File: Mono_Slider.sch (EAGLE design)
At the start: 6 parts

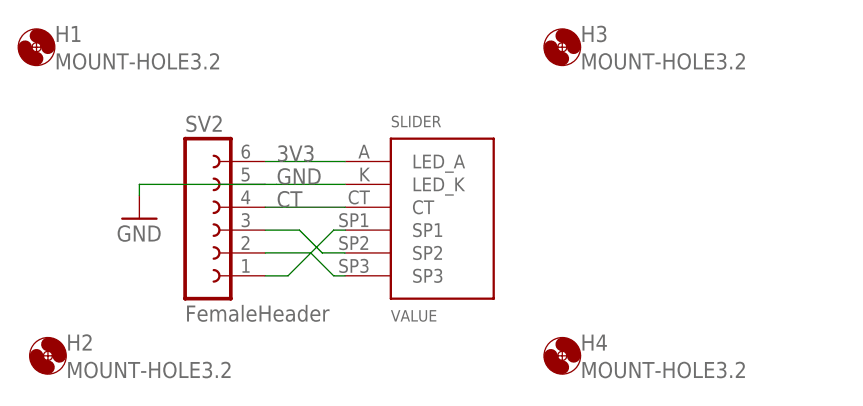
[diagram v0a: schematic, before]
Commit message: Made slider smaller.
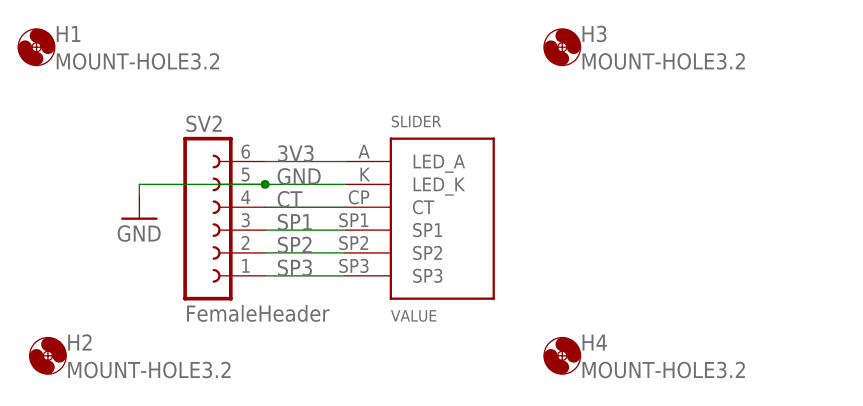
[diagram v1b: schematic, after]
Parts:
- SL1: device SLIDER:SLIDER -> SLIDER:SLIDERSLIDER_SMALL
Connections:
- removed net N$13: SL1.SP3, SV2.2
- removed net N$6: SL1.SP2, SV2.3
- removed net N$7: SL1.SP1, SV2.1
- new net SP1: SL1.SP1, SV2.3
- new net SP2: SL1.SP2, SV2.2
- new net SP3: SL1.SP3, SV2.1
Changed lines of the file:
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@@
 <setting verticaltext="up"/>
 </settings>
-<grid distance="1.27" unitdist="mm" unit="mm" style="dots" multiple="1" display="yes" altdistance="1.27" altunitdist="mm" altunit="mm"/>
+<grid distance="0.1" unitdist="inch" unit="inch" style="lines" multiple="1" display="no" altdistance="0.01" altunitdist="inch" altunit="inch"/>
 <layers>
 <layer number="1" name="Top" color="4" fill="1" visible="no" active="no"/>
@@
 </classes>
 <parts>
-<part name="SL1" library="SLIDER" deviceset="SLIDER" device="" value="SLIDER"/>
 <part name="SV2" library="con-lsta" deviceset="FE06-1" device="" value="FemaleHeader"/>
 <part name="H1" library="holes" deviceset="MOUNT-HOLE" device="3.2"/>
@@
 <part name="H4" library="holes" deviceset="MOUNT-HOLE" device="3.2"/>
 <part name="GND1" library="supply1" deviceset="GND" device=""/>
+<part name="SL1" library="SLIDER" deviceset="SLIDER" device="SLIDER_SMALL" value="SLIDER"/>
 </parts>
 <sheets>
@@
 </plain>
 <instances>
-<instance part="SL1" gate="G$1" x="78.74" y="58.42"/>
 <instance part="SV2" gate="G$1" x="50.8" y="57.15"/>
 <instance part="H1" gate="G$1" x="33.02" y="77.47"/>
@@
 <instance part="H4" gate="G$1" x="91.44" y="43.18"/>
 <instance part="GND1" gate="1" x="44.45" y="58.42"/>
+<instance part="SL1" gate="G$1" x="78.74" y="58.42"/>
 </instances>
 <busses>
@@
 <segment>
 <pinref part="SV2" gate="G$1" pin="6"/>
-<pinref part="SL1" gate="G$1" pin="LED_A"/>
 <wire x1="58.42" y1="64.77" x2="67.31" y2="64.77" width="0.1524" layer="91"/>
 <label x="59.69" y="64.77" size="1.778" layer="95"/>
+<pinref part="SL1" gate="G$1" pin="LED_A"/>
 </segment>
 </net>
@@
 <wire x1="44.45" y1="60.96" x2="44.45" y2="62.23" width="0.1524" layer="91"/>
 <pinref part="SV2" gate="G$1" pin="5"/>
+<label x="59.69" y="62.23" size="1.778" layer="95"/>
+<wire x1="58.42" y1="62.23" x2="67.31" y2="62.23" width="0.1524" layer="91"/>
+<wire x1="44.45" y1="62.23" x2="58.42" y2="62.23" width="0.1524" layer="91"/>
 <pinref part="SL1" gate="G$1" pin="LED_K"/>
-<wire x1="58.42" y1="62.23" x2="59.69" y2="62.23" width="0.1524" layer="91"/>
-<label x="59.69" y="62.23" size="1.778" layer="95"/>
-<wire x1="59.69" y1="62.23" x2="67.31" y2="62.23" width="0.1524" layer="91"/>
-<wire x1="44.45" y1="62.23" x2="58.42" y2="62.23" width="0.1524" layer="91"/>
+<junction x="58.42" y="62.23"/>
 </segment>
 </net>
@@
 <segment>
 <pinref part="SV2" gate="G$1" pin="4"/>
-<pinref part="SL1" gate="G$1" pin="CT"/>
 <wire x1="58.42" y1="59.69" x2="67.31" y2="59.69" width="0.1524" layer="91"/>
 <label x="59.69" y="59.69" size="1.778" layer="95"/>
+<pinref part="SL1" gate="G$1" pin="CT"/>
 </segment>
 </net>
-<net name="N$7" class="0">
+<net name="SP1" class="0">
 <segment>
+<pinref part="SV2" gate="G$1" pin="3"/>
 <pinref part="SL1" gate="G$1" pin="SP1"/>
-<wire x1="67.31" y1="57.15" x2="66.04" y2="57.15" width="0.1524" layer="91"/>
-<wire x1="66.04" y1="57.15" x2="60.96" y2="52.07" width="0.1524" layer="91"/>
-<pinref part="SV2" gate="G$1" pin="1"/>
-<wire x1="60.96" y1="52.07" x2="58.42" y2="52.07" width="0.1524" layer="91"/>
+<wire x1="58.42" y1="57.15" x2="67.31" y2="57.15" width="0.1524" layer="91"/>
+<label x="59.69" y="57.15" size="1.778" layer="95"/>
 </segment>
 </net>
-<net name="N$13" class="0">
+<net name="SP2" class="0">
 <segment>
-<pinref part="SL1" gate="G$1" pin="SP3"/>
-<wire x1="66.04" y1="52.07" x2="67.31" y2="52.07" width="0.1524" layer="91"/>
-<wire x1="66.04" y1="52.07" x2="63.5" y2="54.61" width="0.1524" layer="91"/>
 <pinref part="SV2" gate="G$1" pin="2"/>
-<wire x1="63.5" y1="54.61" x2="58.42" y2="54.61" width="0.1524" layer="91"/>
+<pinref part="SL1" gate="G$1" pin="SP2"/>
+<wire x1="58.42" y1="54.61" x2="67.31" y2="54.61" width="0.1524" layer="91"/>
+<label x="59.69" y="54.61" size="1.778" layer="95"/>
 </segment>
 </net>
-<net name="N$6" class="0">
+<net name="SP3" class="0">
 <segment>
-<pinref part="SL1" gate="G$1" pin="SP2"/>
-<wire x1="67.31" y1="54.61" x2="64.77" y2="54.61" width="0.1524" layer="91"/>
-<pinref part="SV2" gate="G$1" pin="3"/>
-<wire x1="64.77" y1="54.61" x2="62.23" y2="57.15" width="0.1524" layer="91"/>
-<wire x1="62.23" y1="57.15" x2="58.42" y2="57.15" width="0.1524" layer="91"/>
+<pinref part="SV2" gate="G$1" pin="1"/>
+<pinref part="SL1" gate="G$1" pin="SP3"/>
+<wire x1="58.42" y1="52.07" x2="67.31" y2="52.07" width="0.1524" layer="91"/>
+<label x="59.69" y="52.07" size="1.778" layer="95"/>
 </segment>
 </net>
@@
 </sheet>
 </sheets>
+<errors>
+</errors>
 </schematic>
 </drawing>

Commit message: Made pcb smaller to fit in case..
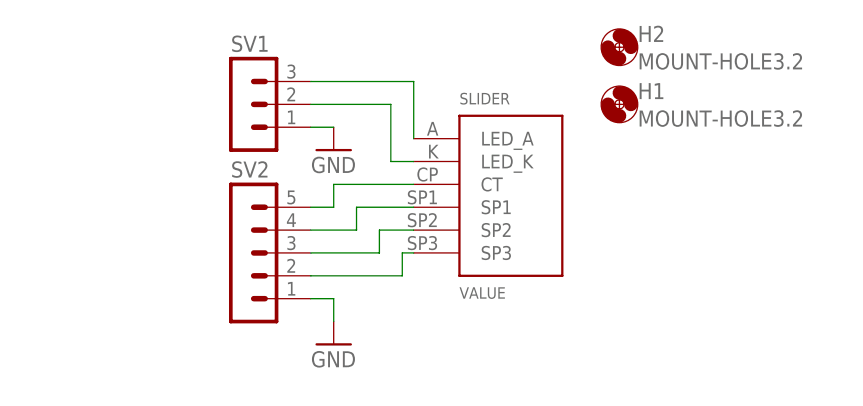
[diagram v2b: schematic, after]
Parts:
- removed H3, H4: MOUNT-HOLE3.2, holes:MOUNT-HOLE3.2
- added SV1: (no value), con-lstb:MA03-1
- SV2: value FemaleHeader -> (none); device con-lsta:FE06-1 -> con-lstb:MA05-1
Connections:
- removed net 3V3: SL1.LED_A, SV2.6
- removed net CT: SL1.CT, SV2.4
- removed net SP1: SL1.SP1, SV2.3
- removed net SP2: SL1.SP2, SV2.2
- removed net SP3: SL1.SP3, SV2.1
- new net N$1: SL1.LED_A, SV1.3
- new net N$2: SL1.LED_K, SV1.2
- new net N$3: SL1.CT, SV2.5
- new net N$4: SL1.SP1, SV2.4
- new net N$5: SL1.SP2, SV2.3
- new net N$6: SL1.SP3, SV2.2
- net GND: now also SV1.1, SV2.1; no longer SL1.LED_K, SV2.5
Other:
- moved on the sheet: H1, H2

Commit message: Changed hatch, silk and clearence
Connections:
- net N$1 renamed A
- net N$2 renamed K
- net N$3 renamed CP
- net N$4 renamed SP1
- net N$5 renamed SP2
- net N$6 renamed SP3
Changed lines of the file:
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@@
 </busses>
 <nets>
-<net name="N$1" class="0">
+<net name="A" class="0">
 <segment>
 <pinref part="SL1" gate="G$1" pin="LED_A"/>
@@
 </segment>
 </net>
-<net name="N$2" class="0">
+<net name="K" class="0">
 <segment>
 <pinref part="SL1" gate="G$1" pin="LED_K"/>
@@
 </segment>
 </net>
-<net name="N$3" class="0">
+<net name="CP" class="0">
 <segment>
 <pinref part="SL1" gate="G$1" pin="CT"/>
@@
 </segment>
 </net>
-<net name="N$4" class="0">
+<net name="SP1" class="0">
 <segment>
 <pinref part="SL1" gate="G$1" pin="SP1"/>
@@
 </segment>
 </net>
-<net name="N$5" class="0">
+<net name="SP2" class="0">
 <segment>
 <pinref part="SL1" gate="G$1" pin="SP2"/>
@@
 </segment>
 </net>
-<net name="N$6" class="0">
+<net name="SP3" class="0">
 <segment>
 <pinref part="SL1" gate="G$1" pin="SP3"/>
